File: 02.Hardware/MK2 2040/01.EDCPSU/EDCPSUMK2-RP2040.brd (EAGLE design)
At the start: 96 x 60.8 mm, 208 parts, among them J1 DX07S016JA1R1500, J6 Display, K1 FLEX CONNECTORES, Q2 2N7002PW, Q4 2N7002PW, Q5 2N7002PW, Q9 2N7002PW, U1 RP2040TR7, U10 IP2721, U11 AP63203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

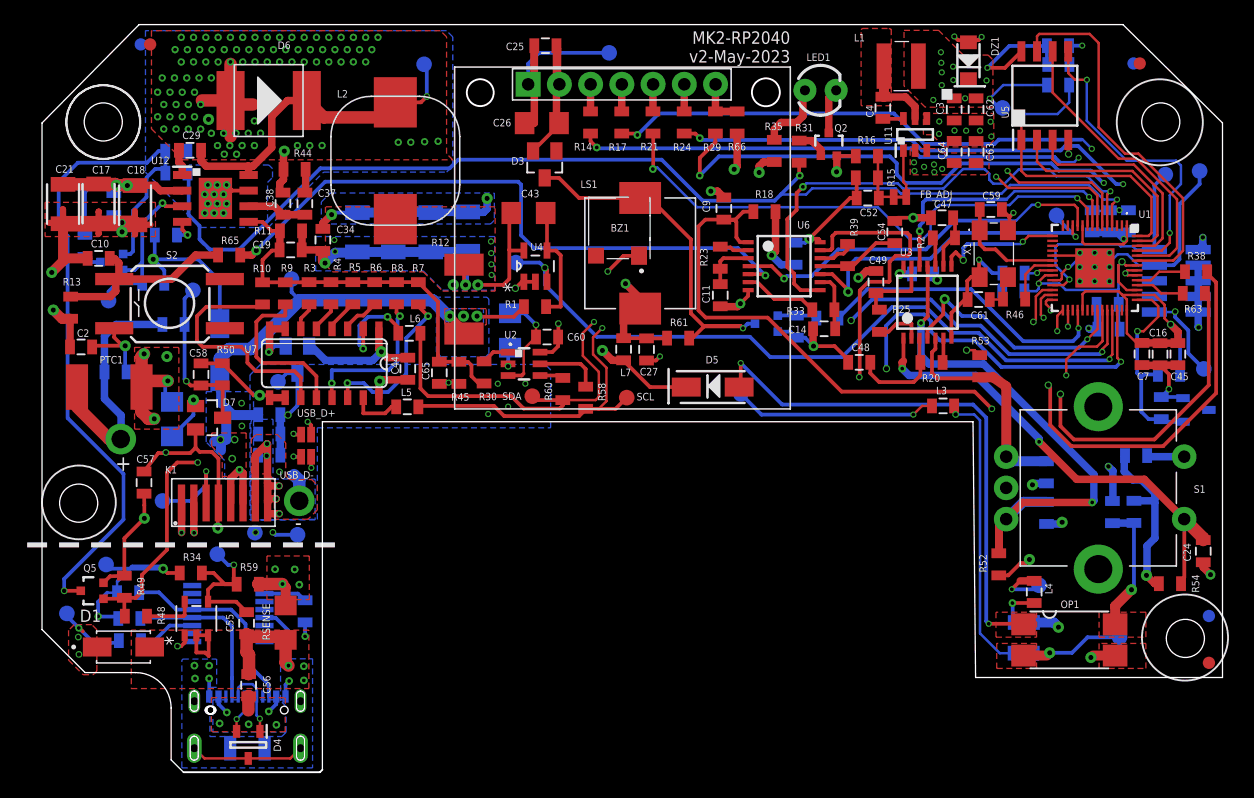
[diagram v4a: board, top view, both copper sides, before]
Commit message: Produccion SETI - Modificaciones menores y generacion de GERBER para fabricacion
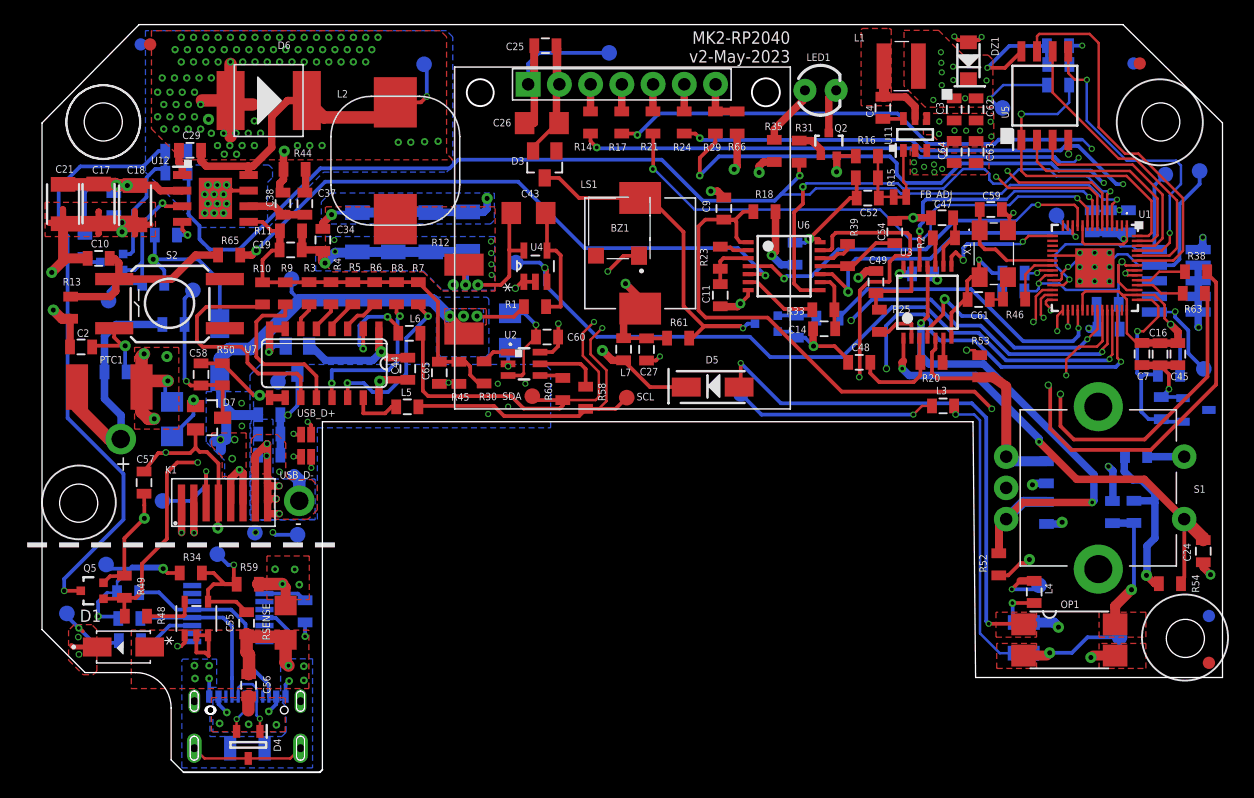
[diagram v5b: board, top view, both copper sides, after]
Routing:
- net PUSH: track 52.2 -> 49.8 mm
- net IN+: track 31.7 -> 33.9 mm
- net N$11: track 5.80 -> 5.06 mm
- net N$65: track 91.3 -> 90.7 mm
- net SDA: track 89.1 -> 89.6 mm

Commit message: Fallo en el I2C. #Issue 15
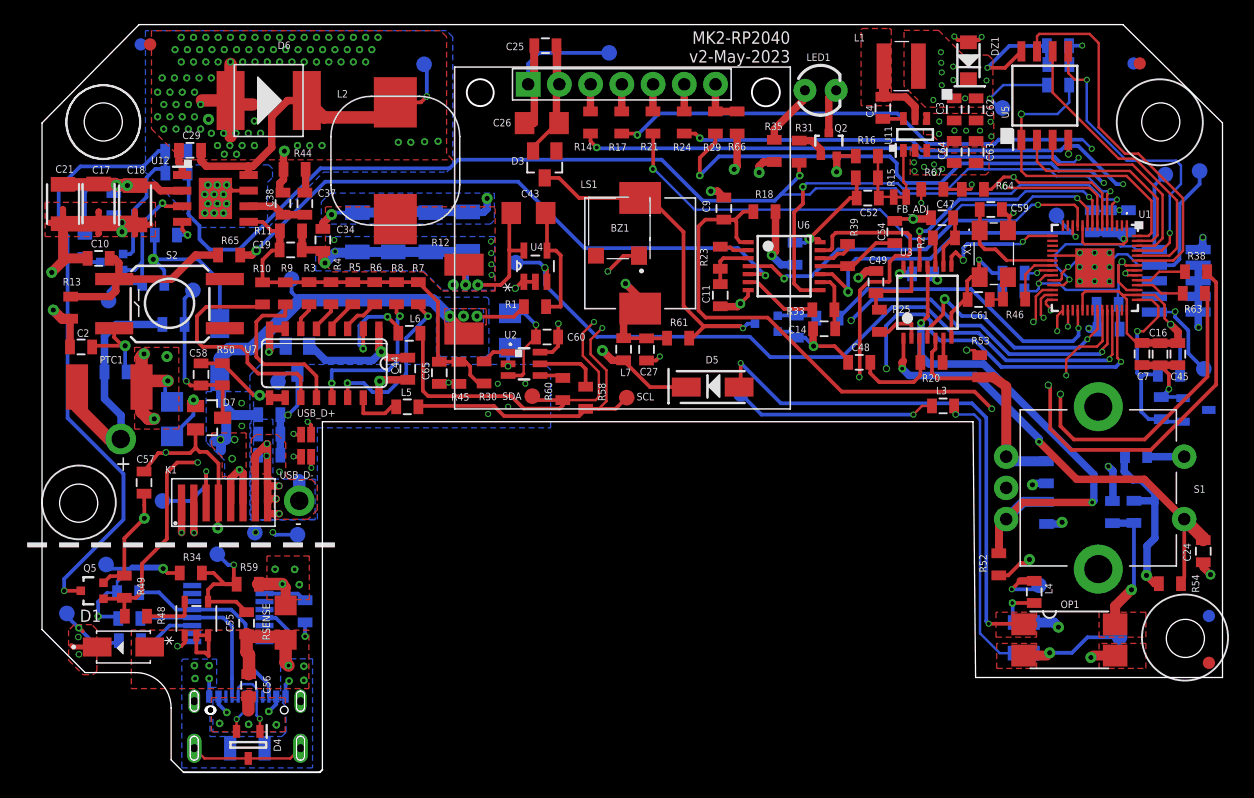
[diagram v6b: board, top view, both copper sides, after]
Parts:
- added R64, R67: 2K2, SparkFun-Resistors:0805
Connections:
- net 3V3MCU: now also R64.2, R67.2
- net SCL: now also R67.1
- net SDA: now also R64.1
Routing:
- net SDA: track 89.6 -> 92.4 mm
- net 3V3MCU: track 171.3 -> 173.9 mm, vias 30 -> 31
- net SCL: track 84.6 -> 87.1 mm, vias 2 -> 3
- net PUSH_FILT: track 41.4 -> 40.1 mm
- net RPUSH_FILT: track 21.8 -> 20.6 mm
- net DSP_RST: track 44.7 -> 43.9 mm
- net GND: track 232.5 -> 231.8 mm

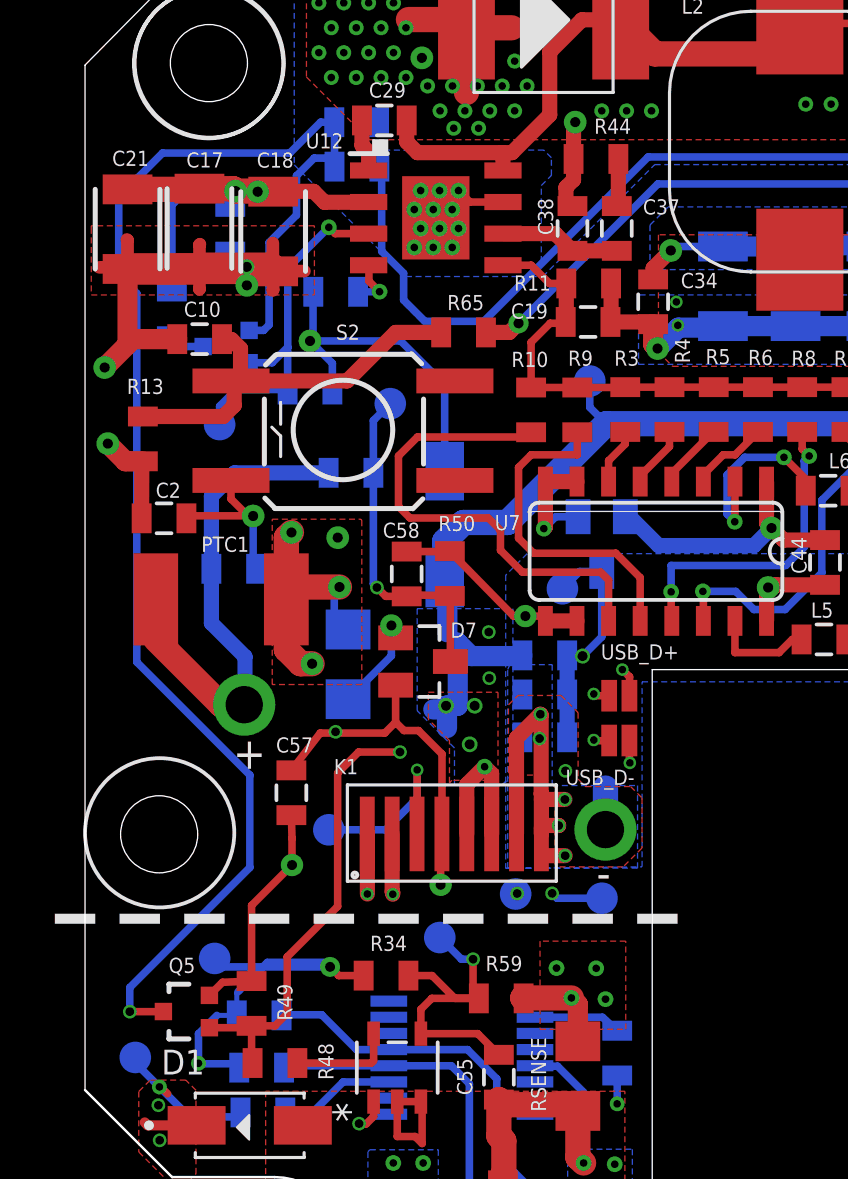
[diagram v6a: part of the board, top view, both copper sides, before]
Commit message: Issue #18
Version 1 de la propuesta de cambio
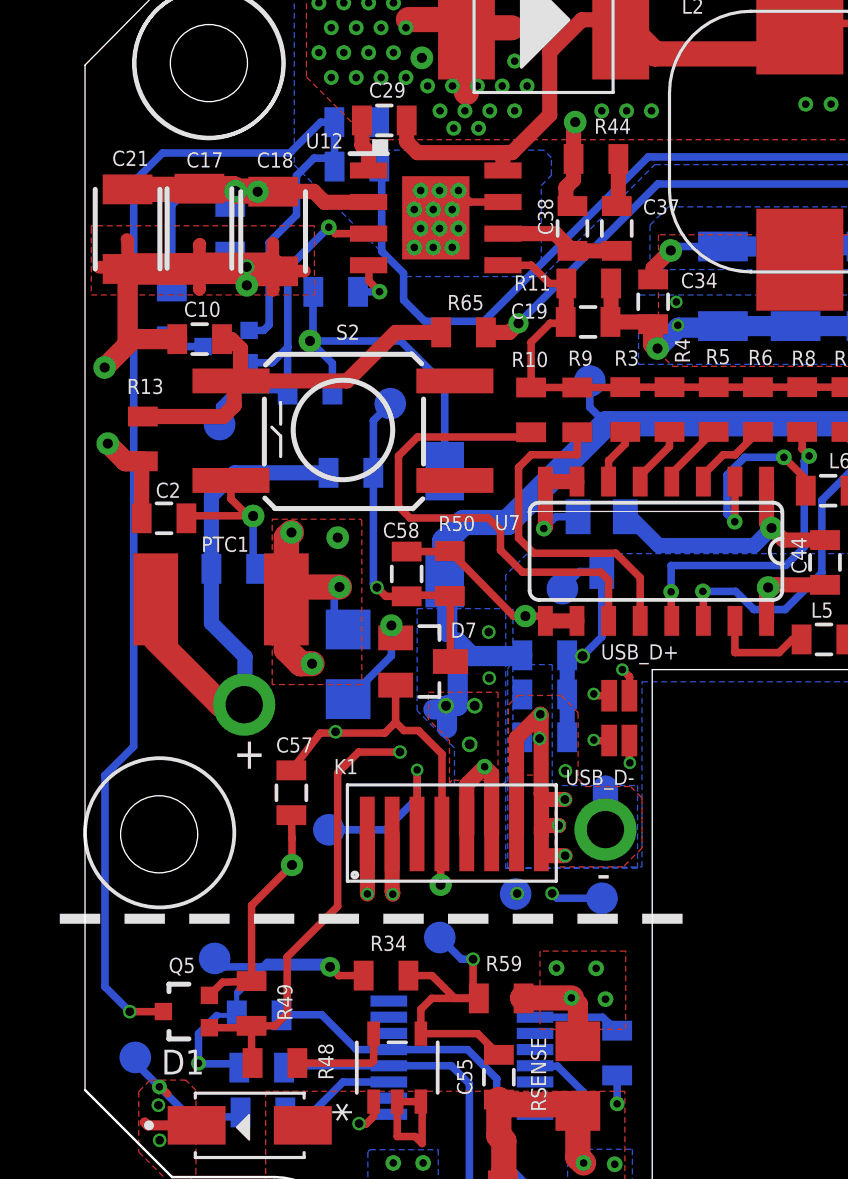
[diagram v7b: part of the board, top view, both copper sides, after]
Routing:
- net SAFETY_EN_DCDC: track 59.3 -> 55.8 mm
- added copper zone on layer 2, net STOP
- added copper zone on layer 2, net STOP1
- added copper zone on layer 15, net STOP2
- added copper zone on layer 15, net STOP3
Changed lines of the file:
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@@
 <drawing>
 <settings>
-<setting alwaysvectorfont="yes"/>
+<setting alwaysvectorfont="no"/>
 <setting keepoldvectorfont="yes"/>
 <setting verticaltext="up"/>
@@
 <grid distance="0.1" unitdist="mm" unit="mm" style="lines" multiple="1" display="no" altdistance="1" altunitdist="mil" altunit="mm"/>
 <layers>
-<layer number="1" name="Top" color="4" fill="1" visible="yes" active="yes"/>
-<layer number="2" name="GND" color="5" fill="1" visible="no" active="yes"/>
+<layer number="1" name="Top" color="4" fill="1" visible="no" active="yes"/>
+<layer number="2" name="GND" color="5" fill="1" visible="yes" active="yes"/>
 <layer number="3" name="Route3" color="4" fill="3" visible="no" active="no"/>
 <layer number="4" name="Route4" color="1" fill="4" visible="no" active="no"/>
@@
 <layer number="13" name="Route13" color="4" fill="5" visible="no" active="no"/>
 <layer number="14" name="Route14" color="1" fill="6" visible="no" active="no"/>
-<layer number="15" name="PWR" color="3" fill="1" visible="no" active="yes"/>
+<layer number="15" name="PWR" color="3" fill="1" visible="yes" active="yes"/>
 <layer number="16" name="Bottom" color="1" fill="1" visible="yes" active="yes"/>
 <layer number="17" name="Pads" color="2" fill="1" visible="yes" active="yes"/>
@@
 <wire x1="37.4" y1="12" x2="37.6" y2="12.2" width="0.1524" layer="20"/>
 <circle x="17.8" y="33.94" radius="3" width="0.1524" layer="21"/>
-<wire x1="13.585" y1="30.485" x2="39.085" y2="30.485" width="0.4064" layer="21" style="shortdash"/>
+<wire x1="13.785" y1="30.485" x2="39.285" y2="30.485" width="0.4064" layer="21" style="shortdash"/>
 <circle x="19.765" y="64.855" radius="3" width="0.1524" layer="21"/>
 <circle x="19.795" y="64.885" radius="3" width="0.1524" layer="21"/>
@@
 <attribute name="NAME" x="77.5281" y="55.0438" size="0.6096" layer="26" font="vector" rot="MR270"/>
 </element>
-<element name="C53" library="SparkFun-Passives" package="0805" value="100n 50v X7R/X5R" x="86.453" y="52.517" smashed="yes" rot="MR0">
-<attribute name="NAME" x="87.215" y="53.3425" size="0.6096" layer="26" font="vector" rot="MR0"/>
+<element name="C53" library="SparkFun-Passives" package="0805" value="100n 50v X7R/X5R" x="86.453" y="52.517" locked="yes" smashed="yes" rot="MR0">
+<attribute name="NAME" x="87.215" y="53.3425" locked="yes" size="0.6096" layer="26" font="vector" rot="MR0"/>
 </element>
 <element name="C54" library="SparkFun-Passives" package="0805" value="1uF 50V X7R" x="84.147" y="55.928" smashed="yes" rot="R270">
@@
 <wire x1="32.5" y1="42.65" x2="33.1128" y2="42.65" width="0.3048" layer="1"/>
 <wire x1="33.1128" y1="42.65" x2="33.3055" y2="42.4573" width="0.3048" layer="1"/>
-<polygon width="0.2032" layer="2" isolate="0.35">
+<polygon width="0.2032" layer="2" isolate="0.35" rank="2">
 <vertex x="13.76" y="25.55"/>
 <vertex x="39.385" y="25.55"/>
@@
 <vertex x="33.09" y="26.04"/>
 <vertex x="36.535" y="26.04"/>
-<vertex x="36.535" y="29.585"/>
-<vertex x="33.09" y="29.585"/>
+<vertex x="36.535" y="29.185"/>
+<vertex x="33.09" y="29.185"/>
 </polygon>
 <via x="33.752" y="28.502" extent="1-16" drill="0.3048" diameter="0.635"/>
@@
 <wire x1="23.468" y1="40.735" x2="23.928" y2="40.735" width="1.016" layer="1"/>
 <via x="21.74" y="59.71" extent="1-16" drill="0.4064" diameter="0.9"/>
-<polygon width="0.254" layer="15" isolate="0.254" rank="2">
-<vertex x="18.91" y="29.77"/>
+<polygon width="0.254" layer="15" isolate="0.254" rank="3">
+<vertex x="18.91" y="31.27"/>
 <vertex x="18.91" y="61.59"/>
 <vertex x="26.03" y="61.59"/>
@@
 <vertex x="85.58" y="61.96"/>
 <vertex x="88.93" y="61.96"/>
-<vertex x="88.93" y="29.77"/>
+<vertex x="88.93" y="31.27"/>
 </polygon>
 <contactref element="U11" pad="2"/>
@@
 <wire x1="79.4336" y1="49.1336" x2="80.14" y2="49.84" width="0.2032" layer="15"/>
 <wire x1="80.14" y1="49.84" x2="84.45" y2="49.84" width="0.2032" layer="15"/>
-<wire x1="85.2014" y1="50.5914" x2="85.2014" y2="53.1998125" width="0.2032" layer="15"/>
+<wire x1="85.2014" y1="50.5914" x2="85.2014" y2="53.1998125" width="0.2032" layer="15" locked="yes"/>
 <wire x1="71.23280625" y1="49.1336" x2="79.4336" y2="49.1336" width="0.2032" layer="15"/>
 <wire x1="84.45" y1="49.84" x2="85.2014" y2="50.5914" width="0.2032" layer="15"/>
@@
 <wire x1="36.5201" y1="46.6441" x2="36.7001" y2="46.6441" width="0.6096" layer="16"/>
 <wire x1="41.691" y1="45.486" x2="42.396" y2="46.191" width="0.6096" layer="16"/>
-<polygon width="0.4064" layer="15" isolate="0.3048" rank="3">
+<polygon width="0.4064" layer="15" isolate="0.3048" rank="4">
 <vertex x="14.55" y="40.736"/>
 <vertex x="14.55" y="65.441"/>
@@
 <wire x1="24.59" y1="48.41" x2="20.815" y2="48.41" width="0.6096" layer="16"/>
 <wire x1="20.815" y1="48.41" x2="19.879" y2="47.474" width="0.6096" layer="16"/>
-<polygon width="0.1524" layer="15" isolate="0.254">
+<polygon width="0.1524" layer="15" isolate="0.254" rank="2">
 <vertex x="14.2" y="40.87"/>
 <vertex x="14.2" y="22.35"/>
 <vertex x="25.85" y="10.7"/>
 <vertex x="38.7" y="10.7"/>
-<vertex x="38.7" y="29.7"/>
-<vertex x="38.6" y="29.8"/>
-<vertex x="22.68" y="29.8"/>
+<vertex x="38.7" y="29.1"/>
+<vertex x="22.68" y="29.1"/>
 <vertex x="22.68" y="40.87"/>
 </polygon>
@@
 <wire x1="24.82" y1="62.504" x2="24.83" y2="62.494" width="0.3048" layer="16"/>
 <wire x1="24.83" y1="62.494" x2="24.83" y2="60.72" width="0.3048" layer="16"/>
-<wire x1="16.88" y1="40.805" x2="21.425" y2="36.26" width="0.3048" layer="16"/>
-<wire x1="21.425" y1="36.26" x2="21.425" y2="32.545" width="0.3048" layer="16"/>
-<wire x1="21.425" y1="32.545" x2="16.6" y2="27.72" width="0.3048" layer="16"/>
-<wire x1="16.6" y1="27.72" x2="16.6" y2="26.75" width="0.3048" layer="16"/>
 <via x="16.6" y="26.75" extent="1-16" drill="0.35"/>
 <wire x1="16.6" y1="26.75" x2="17.955" y2="26.75" width="0.3048" layer="1"/>
@@
 <wire x1="24.27" y1="62.504" x2="23.03" y2="61.264" width="0.3048" layer="16"/>
 <wire x1="23.03" y1="61.264" x2="17.914" y2="61.264" width="0.3048" layer="16"/>
-<wire x1="17.914" y1="61.264" x2="16.155" y2="59.505" width="0.3048" layer="16"/>
-<wire x1="16.155" y1="59.505" x2="16.155" y2="56.35" width="0.3048" layer="16"/>
-<wire x1="16.88" y1="55.625" x2="16.88" y2="40.805" width="0.3048" layer="16"/>
-<wire x1="16.155" y1="56.35" x2="16.88" y2="55.625" width="0.3048" layer="16"/>
+<wire x1="17.914" y1="61.264" x2="16.755" y2="60.105" width="0.3048" layer="16"/>
 <wire x1="21.395" y1="54.136" x2="21.976" y2="54.136" width="0.3048" layer="16"/>
 <wire x1="21.976" y1="54.136" x2="22.2004" y2="54.3604" width="0.3048" layer="16"/>
@@
 <wire x1="24.49" y1="61.06" x2="24.83" y2="60.72" width="0.3048" layer="16"/>
 <wire x1="24.49" y1="61.06" x2="24.01" y2="61.06" width="0.3048" layer="16"/>
+<wire x1="16.755" y1="60.105" x2="16.755" y2="37.405" width="0.3048" layer="16"/>
+<wire x1="16.755" y1="37.405" x2="15.6" y2="36.25" width="0.3048" layer="16"/>
+<wire x1="15.6" y1="36.25" x2="15.6" y2="27.75" width="0.3048" layer="16"/>
+<wire x1="16.6" y1="26.75" x2="15.6" y2="27.75" width="0.3048" layer="16"/>
 </signal>
 <signal name="IN_OVC">
@@
 <wire x1="108.02" y1="47.93" x2="108.02" y2="46.06" width="0.3048" layer="16"/>
 </signal>
+<signal name="STOP">
+<polygon width="0.1524" layer="2" pour="cutout" isolate="0.254">
+<vertex x="13.1" y="31.7"/>
+<vertex x="25.4" y="31.7"/>
+<vertex x="25.4" y="29.1"/>
+<vertex x="13.1" y="29.1"/>
+</polygon>
+</signal>
+<signal name="STOP1">
+<polygon width="0.1524" layer="2" pour="cutout" isolate="0.254">
+<vertex x="28.4" y="31.7"/>
+<vertex x="34.1" y="31.7"/>
+<vertex x="34.1" y="29.1"/>
+<vertex x="28.4" y="29.1"/>
+</polygon>
+</signal>
+<signal name="STOP2">
+<polygon width="0.1524" layer="15" pour="cutout" isolate="0.254">
+<vertex x="21" y="31.7"/>
+<vertex x="34.1" y="31.7"/>
+<vertex x="34.1" y="29.1"/>
+<vertex x="21" y="29.1"/>
+</polygon>
+</signal>
+<signal name="STOP3">
+<polygon width="0.1524" layer="15" pour="cutout" isolate="0.254">
+<vertex x="14.1" y="31.6"/>
+<vertex x="16.4" y="31.6"/>
+<vertex x="16.4" y="29"/>
+<vertex x="14.1" y="29"/>
+</polygon>
+</signal>
 </signals>
